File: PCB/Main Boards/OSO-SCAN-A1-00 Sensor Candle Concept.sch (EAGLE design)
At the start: 58 parts, among them J1 10118193-0001LF, Q1 DMG341, SW2 SPST_TACT-KMR2, U1 AP2112-3.3, U2 ATSAMD11D14A-MUT, U3 LIS2DHTR, U4 AP2112-1.8

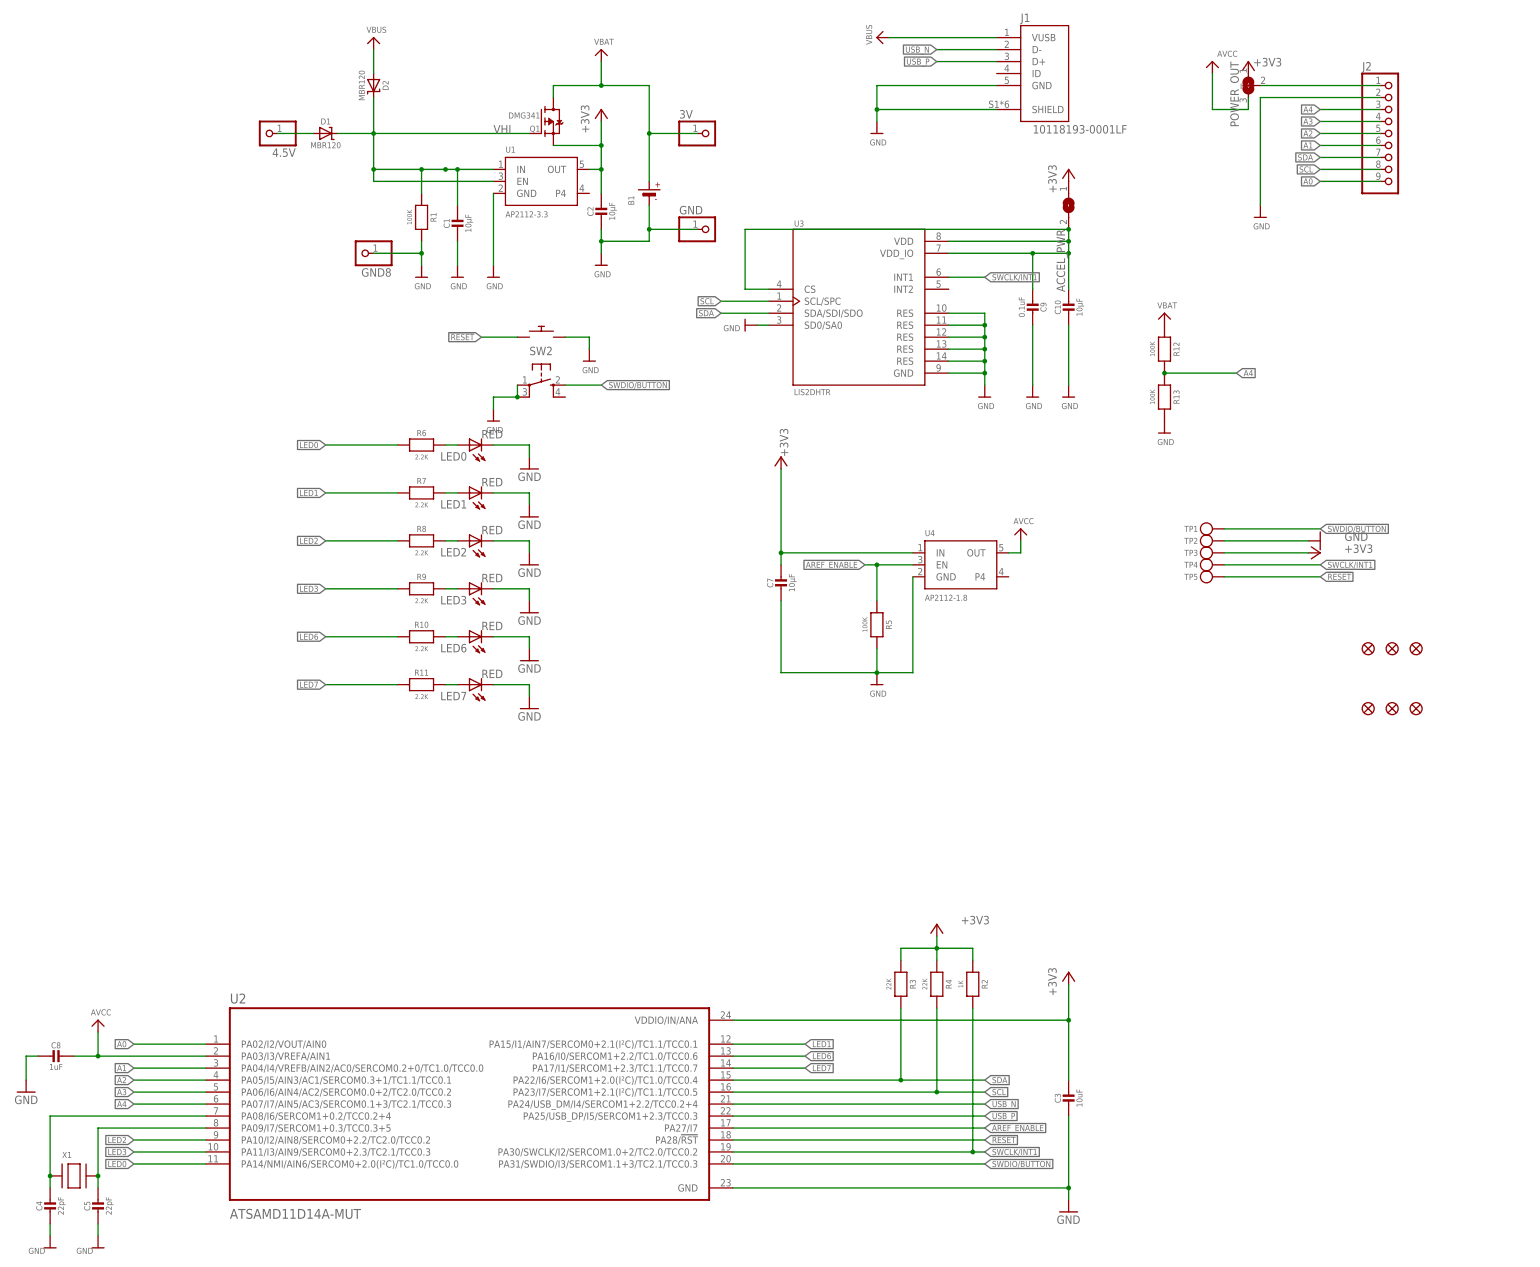
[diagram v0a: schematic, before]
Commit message: organize schematic, update some values
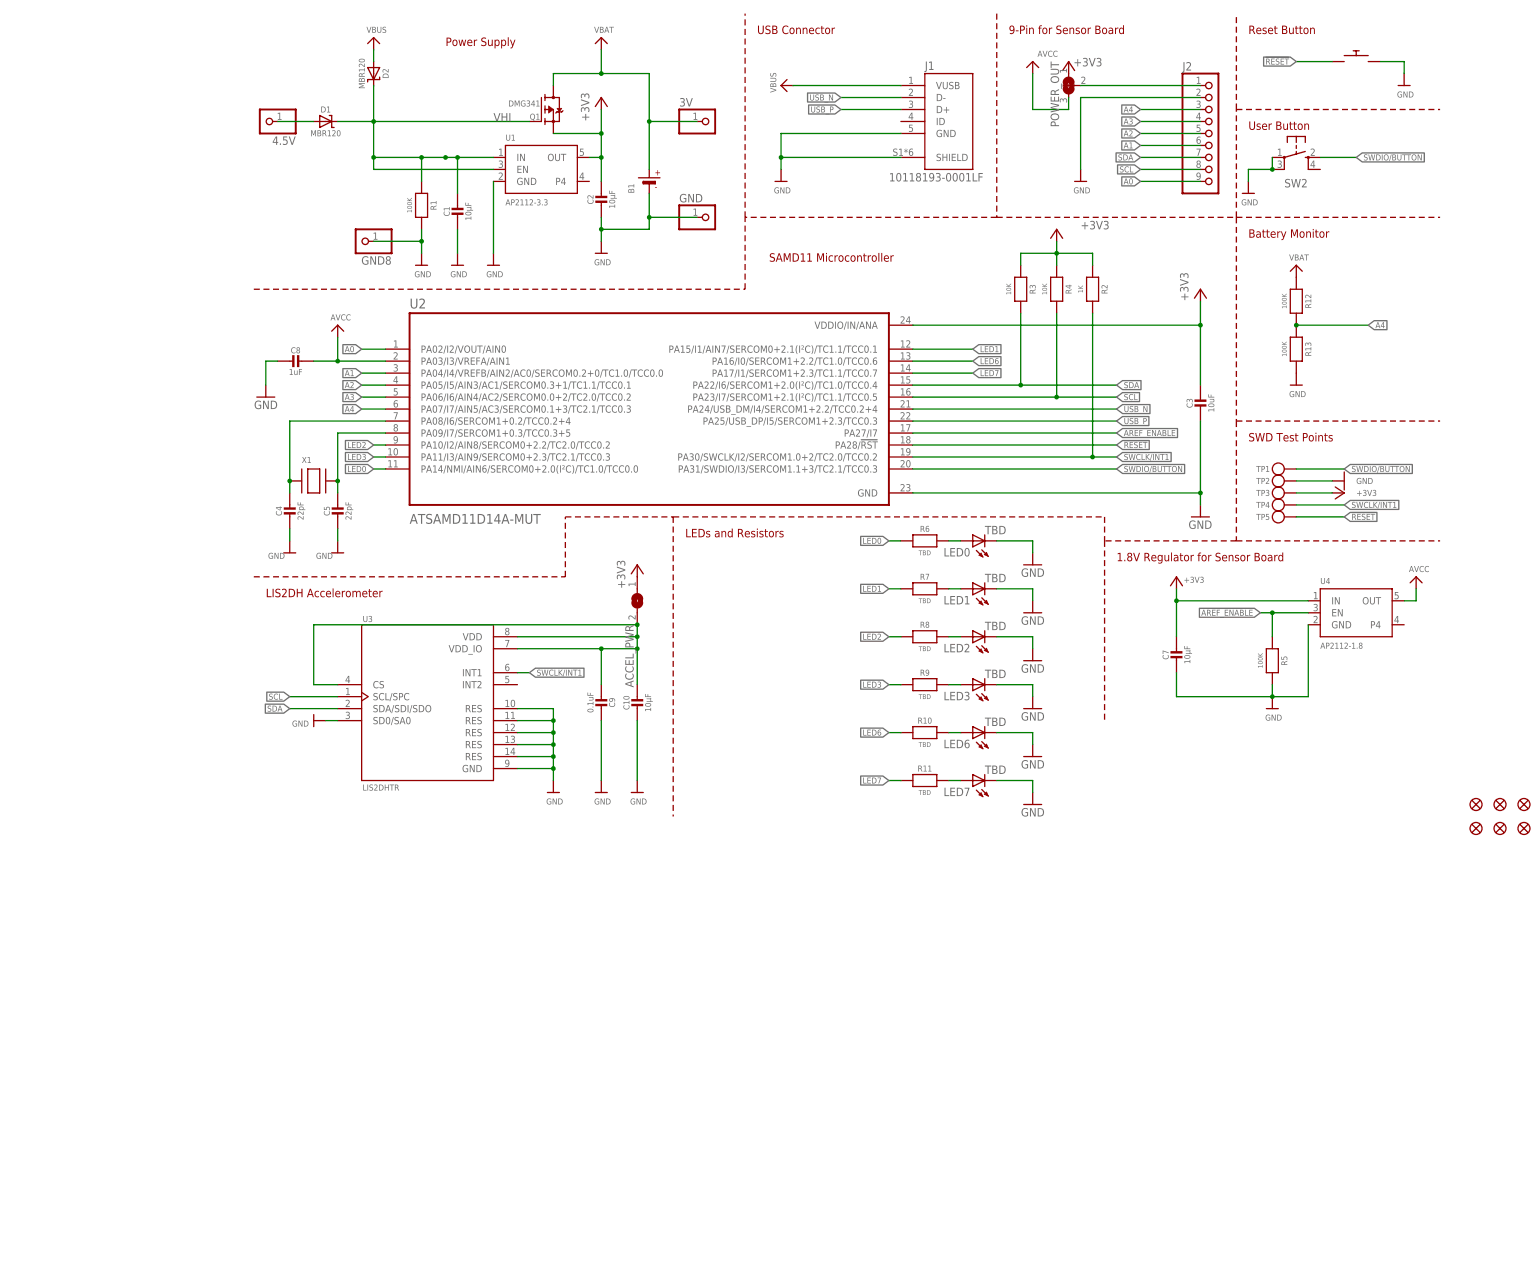
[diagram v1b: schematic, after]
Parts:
- LED0, LED1, LED2, LED3, LED6, LED7: value RED -> TBD
- R10, R11, R6, R7, R8, R9: value 2.2K -> TBD
- R3, R4: value 22K -> 10K
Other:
- note added: "1.8V Regulator for Sensor Board"
- note added: "9-Pin for Sensor Board"
- note added: "Battery Monitor"
- note added: "LEDs and Resistors"
- note added: "LIS2DH Accelerometer"
- note added: "Power Supply"
- note added: "Reset Button"
- note added: "SAMD11 Microcontroller"
- note added: "SWD Test Points"
- note added: "These values are all TBD — by you! It'll be different depending on what color and type of LED you want to use, as well as how you power the board. Note that white or blue LED's will not work with a coin cell or two AA's; you'll need to power the board via USB or the 4.5V pin. The only hard and fast rule here is, don't draw more than 7 mA from any pin. Also keep in mind that you can PWM these for 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"
- note added: "USB Connector"
- note added: "User Button"
- moved on the sheet: 3V, 4.5V, ACCEL_PWR, B1, C1, C10, C2, C3, C4, C5, C7, C8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
